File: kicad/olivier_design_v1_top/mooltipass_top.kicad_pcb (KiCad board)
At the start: 2 copper layers, 31 parts, among them K1 CONN_3, P1 CONN_1, P2 CONN_1, P3 CONN_1, P4 CONN_1, U1 CON_STACK_9, U2 AT42QT2120

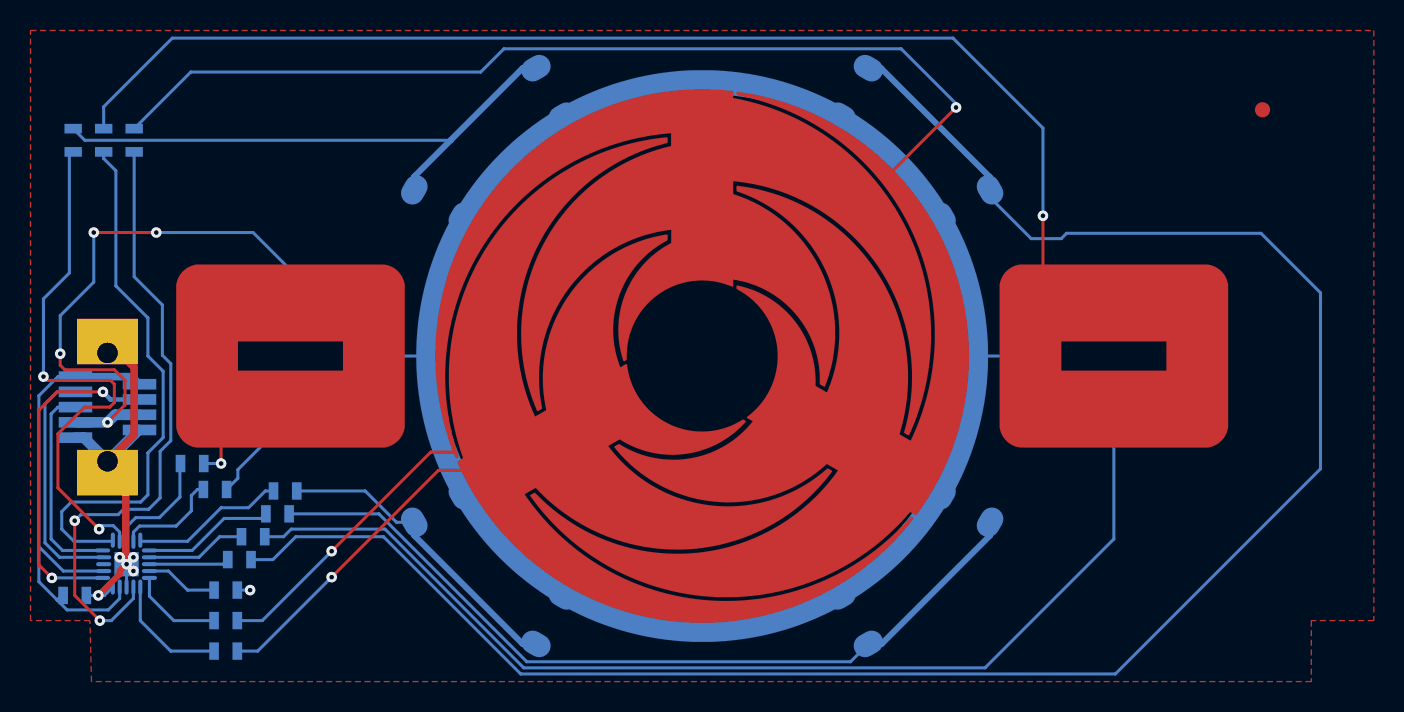
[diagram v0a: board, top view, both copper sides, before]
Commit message: update top PCB for Olivier's design
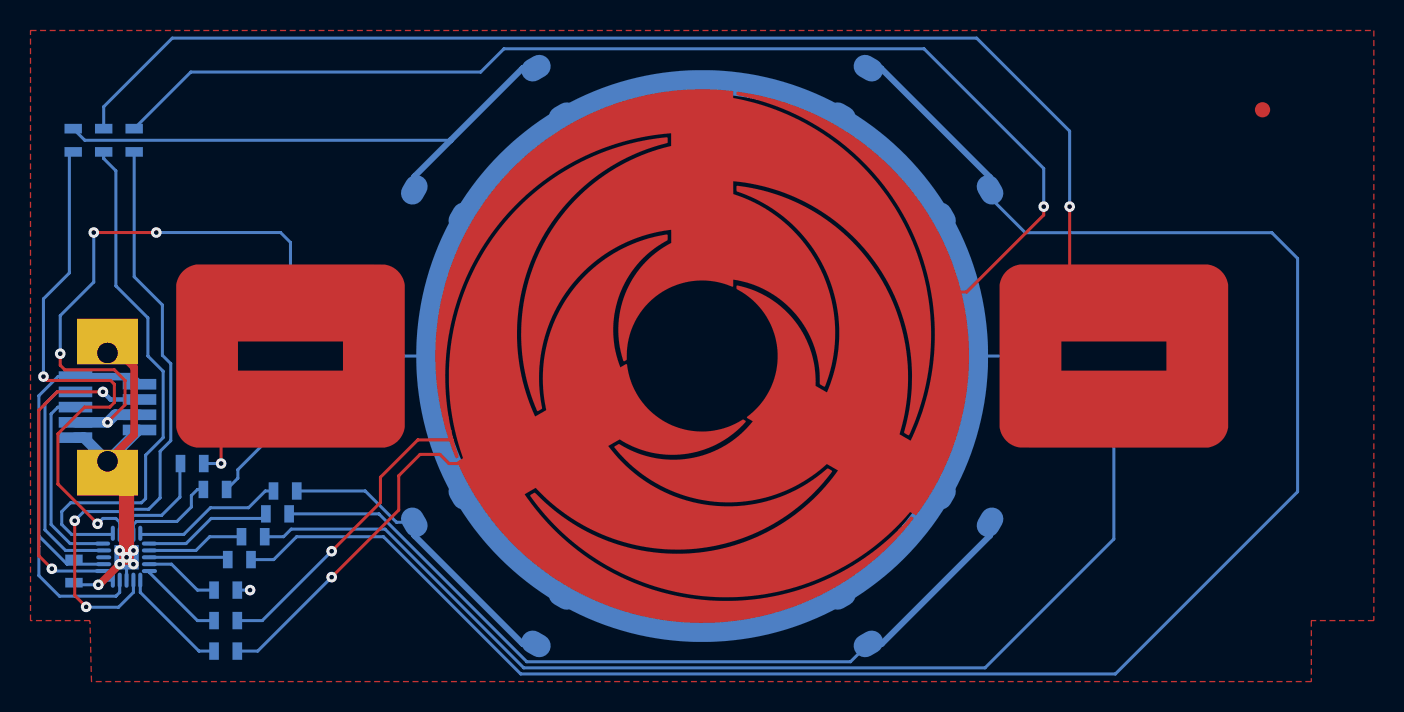
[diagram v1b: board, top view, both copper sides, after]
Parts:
- removed the VAL at (188.2, 148.1)
- added VAL: soldermask_diff, soldermask_diff, F.Cu at (188.2, 148.2)
- moved C1 1.60 mm to (147.1, 162.2), turned to 270 degrees
- moved U2 0.45 mm to (150.5, 161.3)
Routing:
- net /WHEEL0: track 86.2 -> 89.1 mm
- net /WHEEL1: track 21.6 -> 24.1 mm
- net /KEY11: track 83.9 -> 85.6 mm
- net GND: track 34.0 -> 32.8 mm, vias 5 -> 6
- net +5V: track 32.1 -> 30.9 mm
- net N-000004: track 128.4 -> 127.3 mm
- net /LED_CAT: track 157.8 -> 158.8 mm
- net /nCHANGE: track 13.7 -> 13.0 mm
- net /I2C_SCL: track 15.7 -> 15.0 mm
- net N-0000023: track 7.87 -> 7.23 mm
- net /I2C_SDA: track 22.1 -> 21.5 mm
- net N-0000024: track 41.0 -> 40.5 mm

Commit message: final PCBs!
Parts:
- removed the VAL at (188.2, 148.2)
- added VAL: soldermask_light, soldermask_light, F.Cu at (188.2, 145.7)
- C1: value C -> 100nF
- R1, R10, R11, R12, R2, R9: value R -> 10k
- R13, R14, R15, R16: value R -> 330
- R17, R18: value R -> 620
- moved D4 1.31 mm to (171.6, 159.3), turned to 33.8 degrees
- moved D6 1.31 mm to (177.1, 131.5), turned to 303.8 degrees
- moved D2 1.31 mm to (199.4, 164.8), turned to 123.8 degrees
- moved D3 1.31 mm to (177.1, 164.8), turned to 56.2 degrees
- moved D5 1.31 mm to (171.6, 137.0), turned to 326.2 degrees
- moved D7 1.31 mm to (199.4, 131.5), turned to 236.2 degrees
- moved D8 1.31 mm to (204.9, 137.0), turned to 213.8 degrees
- moved D1 1.31 mm to (204.9, 159.3), turned to 146 degrees
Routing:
- net /LED_CAT: track 158.8 -> 164.1 mm
- net N-000003: track 36.9 -> 33.8 mm
- net N-000004: track 127.3 -> 125.3 mm
- net N-000001: track 20.4 -> 18.5 mm
- net N-000009: track 54.3 -> 52.8 mm
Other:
- rule pad_to_mask_clearance: 0 -> 0.15
- board text added: "Mooltipass M.Stephan / limpkin For Olivier's design Licensed under CERN OHL V1.2"

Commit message: update top gerbers
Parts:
- R13, R14, R15, R16: value 330 -> 390
- R17, R18: value 620 -> 750

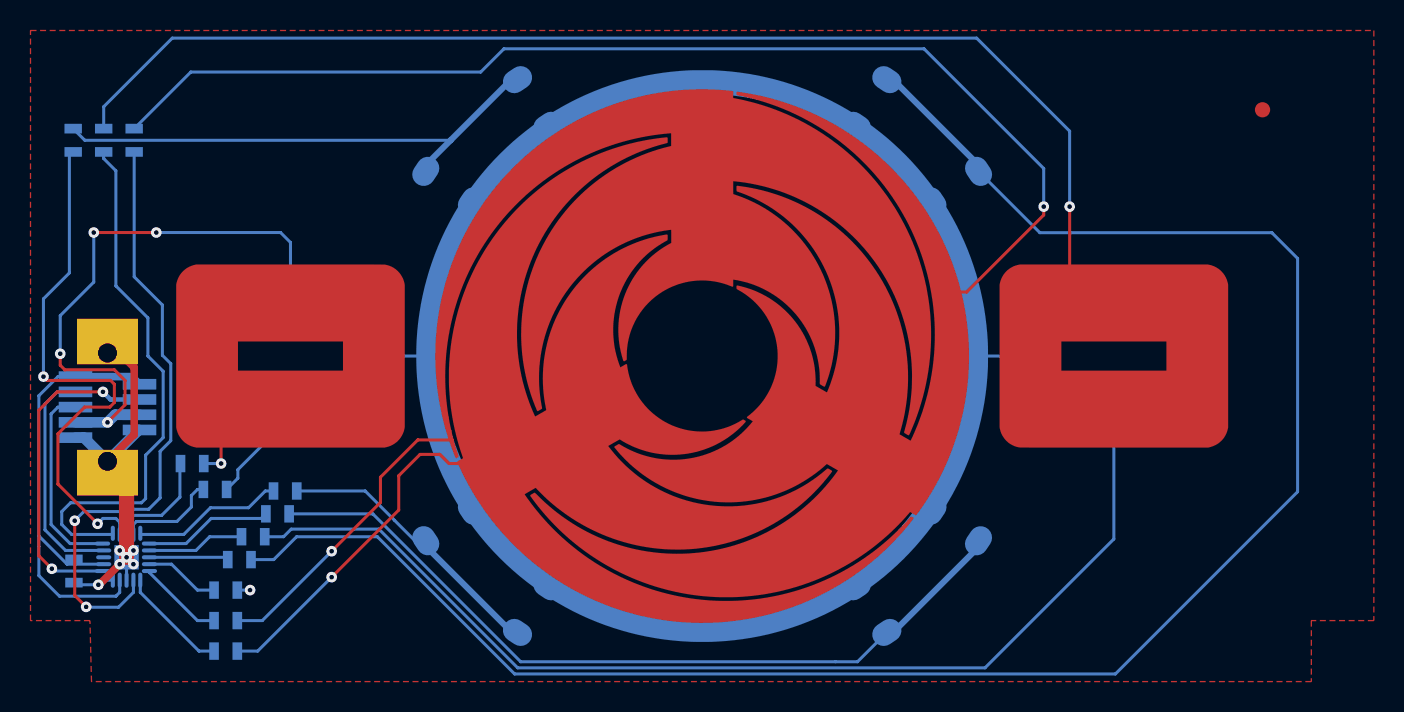
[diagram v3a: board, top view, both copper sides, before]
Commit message: 10k touch resistors, slots added on gerbers
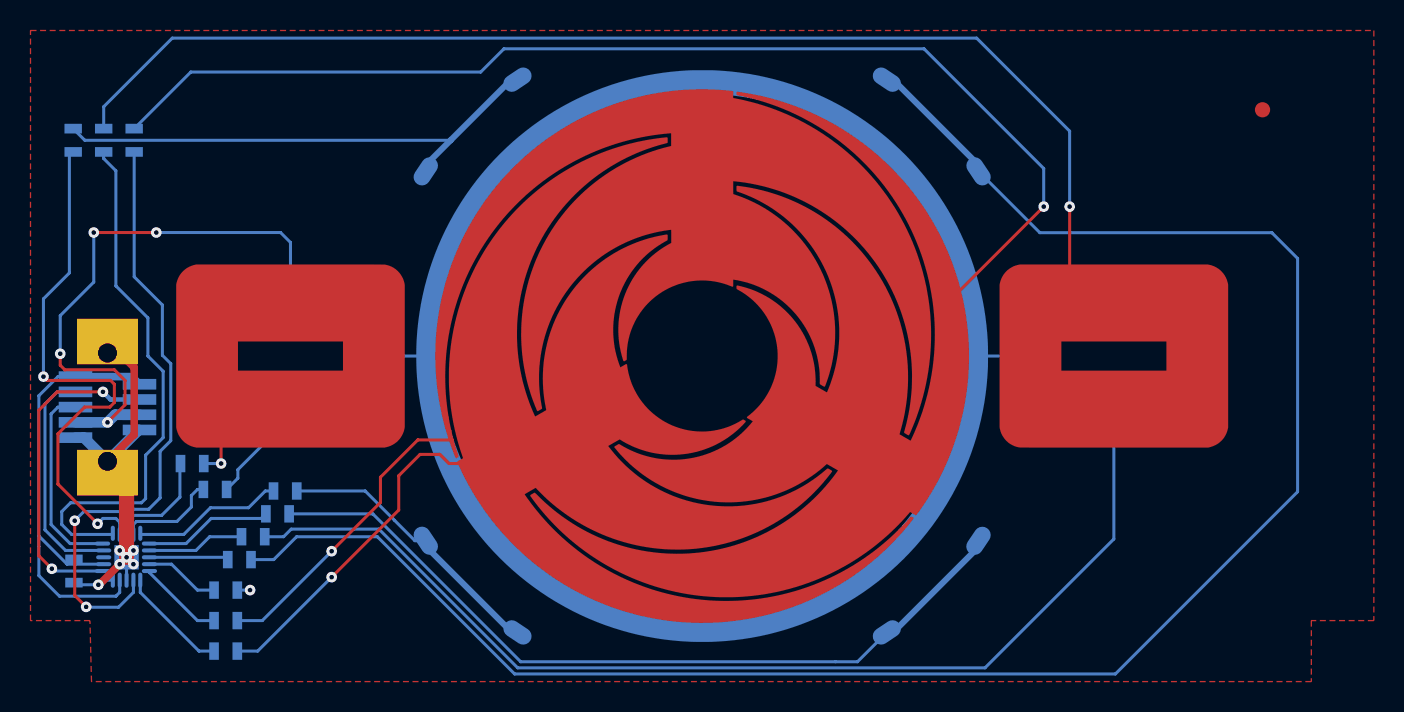
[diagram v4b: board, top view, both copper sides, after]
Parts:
- added VAL: REF, mooltipass_top_slot_drill, F.Cu at (188.2, 148.1)
- R9: value 10k -> 4k7
